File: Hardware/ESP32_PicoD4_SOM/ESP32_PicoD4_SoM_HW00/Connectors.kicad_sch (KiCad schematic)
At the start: 4 parts, among them J101 DF40C-60DP-0.4V(51)

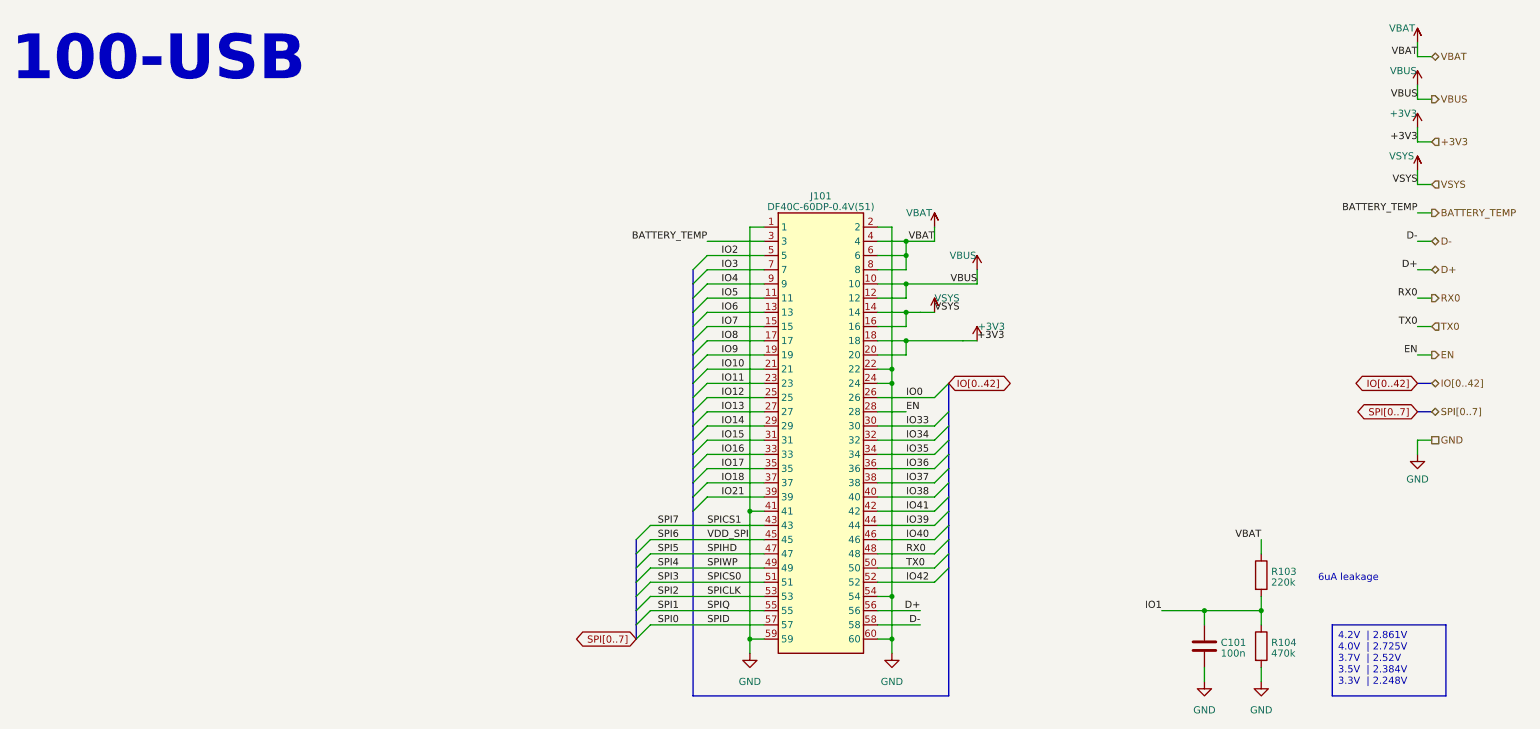
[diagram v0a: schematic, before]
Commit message: First version of schematic Connections
Done according to definition in pinout.xlsx (available on master)
Renaming ESP_... to ESP32_...
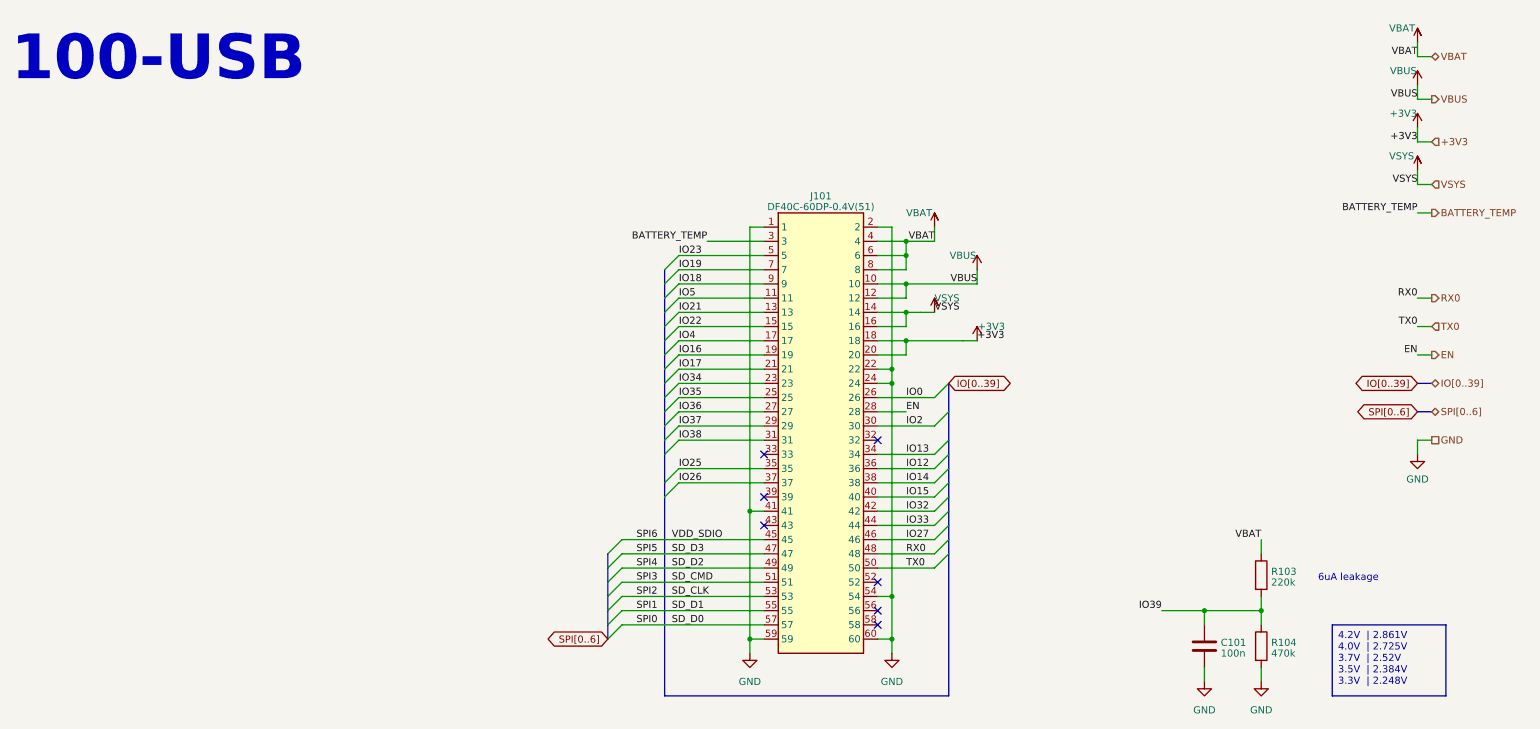
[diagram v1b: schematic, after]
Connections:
- net IO1 is gone; now on net IO39: C101.1, R103.2, R104.1
- net IO10 is gone; now on net IO17: J101.21
- net IO11 is gone; now on net IO34: J101.23
- net IO6 is gone; now on net IO21: J101.13
- net IO8 is gone; now on net IO4: J101.17
- net IO9 is gone; now on net IO16: J101.19
- net IO12: now also J101.36; no longer J101.25
- net IO13: now also J101.34; no longer J101.27
- net IO14: now also J101.38; no longer J101.29
- net IO15: now also J101.40; no longer J101.31
- net IO16: no longer J101.33
- net IO17: no longer J101.35
- net IO18: now also J101.9; no longer J101.37
- net IO2: now also J101.30; no longer J101.5
- net IO21: no longer J101.39
- net IO33: now also J101.44; no longer J101.30
- net IO34: no longer J101.32
- net IO35: now also J101.25; no longer J101.34
- net IO36: now also J101.27; no longer J101.36
- net IO37: now also J101.29; no longer J101.38
- net IO38: now also J101.31; no longer J101.40
- net IO39: no longer J101.44
- net IO4: no longer J101.9
- net D+: no longer names the net of J101.56
- net D-: no longer names the net of J101.58
- net IO3 renamed IO19
- net IO40 renamed IO27
- net IO41 renamed IO32
- net IO42: no longer names the net of J101.52
- net IO7 renamed IO22
- net SPI0 renamed SD_D0
- net SPI1 renamed SD_D1
- net SPI2 renamed SD_CLK
- net SPI3 renamed SD_CMD
- net SPI4 renamed SD_D2
- net SPI5 renamed SD_D3
- net SPI7: no longer names the net of J101.43
- new net IO23: J101.5
- new net IO25: J101.35
- new net IO26: J101.37
- no-connect marks 0 -> 7
